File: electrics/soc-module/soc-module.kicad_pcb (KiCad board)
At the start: 2 copper layers, 56 x 30.4 mm, 19 parts, among them J1 Micro_SD, J2 East, J3 West, SW1 Prog, SW2 Reset, U1 ATECC608A-SSHDA, U2 ESP32-WROVER-IE-16MB

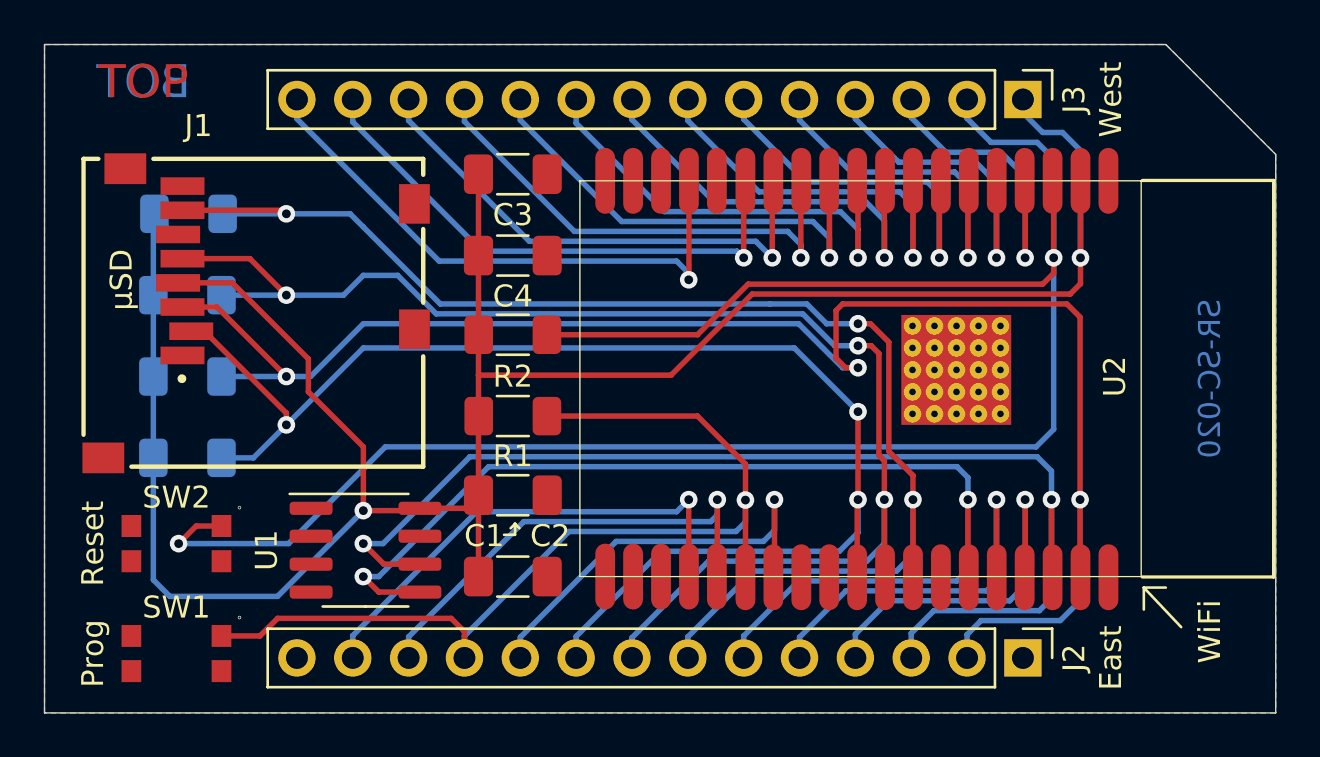
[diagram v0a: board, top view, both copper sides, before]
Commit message: Feature/rtc for soc module (#10)
* Remove outdated files to clean things up

* Added missing part numbers for metering module

* Added 6 position screw terminal

* Added "mieterstrom" module

* Throw generated XML files out of version control

* Add "mieterstrom" module to local build

* Add "Mieterstrom" module to documentation

* Added "Mieterstrom" module to CI/CD

* Added optional RTC to SoC module
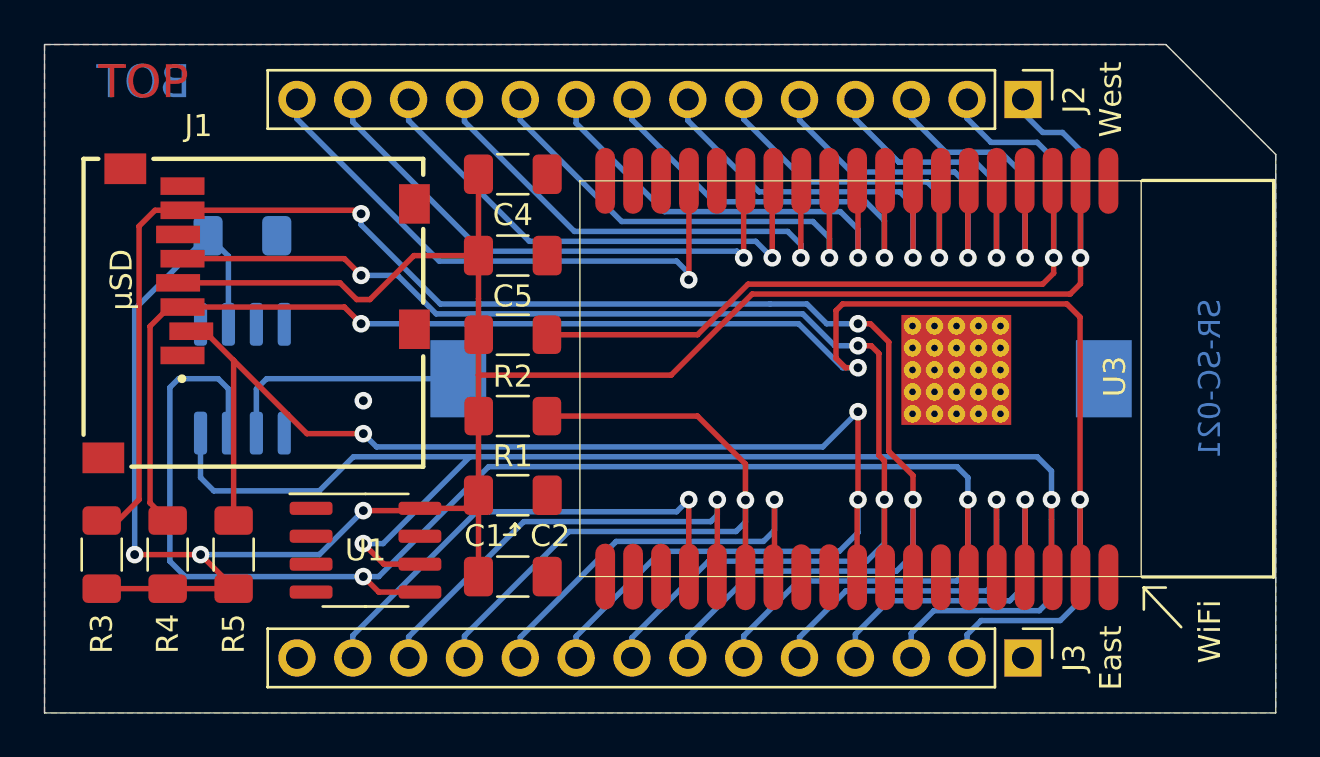
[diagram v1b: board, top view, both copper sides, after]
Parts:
- removed the R4 at (126.5, 91.7)
- removed SW1: Prog, footprints:SW4SMD_63X161LS
- removed SW2: Reset, footprints:SW4SMD_63X161LS
- added BT1: CR2023, Battery:BatteryHolder_Keystone_1058_1x2032, B.Cu at (153.5, 95.5)
- added C3: 100nF, Capacitor_SMD:C_1206_3216Metric_Pad1.33x1.80mm_HandSolder, B.Cu at (129.0, 89.0)
- added U2: DS3231MZ, Package_SO:SOIC-8_3.9x4.9mm_P1.27mm, B.Cu at (129.0, 95.5)
- R3: moved to F.Cu
- R4: renamed from R5; moved to F.Cu
- R5: renamed from R6; moved to F.Cu
- moved R3 16.0 mm to (122.6, 103.5), turned to -90 degrees
- moved R4 8.15 mm to (125.6, 103.5), turned to -90 degrees
- moved R5 4.88 mm to (128.6, 103.5), turned to -90 degrees
- renumbered C3 to C4, C4 to C5, G2 to G1, G1 to G2, J3 to J2, J2 to J3, U2 to U3
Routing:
- net Chip_PU: track 90.8 -> 38.8 mm, vias 2 -> 1
- net IO21: track 53.1 -> 75.2 mm
- net IO22: track 54.0 -> 69.1 mm
- net IO19: track 64.2 -> 78.4 mm
- net IO0: track 45.4 -> 32.3 mm
- net Net-(BT1-Pad1): track 0.00 -> 11.4 mm
- net +3V3: track 110.2 -> 121.2 mm, vias 2 -> 4
- net IO23: track 75.2 -> 81.3 mm
- net IO18: track 63.9 -> 60.2 mm
- net IO5: track 63.7 -> 65.6 mm
- net GND: vias 0 -> 1
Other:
- board text added: "Inoa Satellite v2.0 GrayC GmbH https://docs.inoa.io"
- board text added: "SR-SC-021"
- board text removed: "SPI PullUps"
- board text removed: "SR-SC-020"
- board text removed: "Satellite SoC Module v2.0 GrayC GmbH https://docs.inoa.io"
